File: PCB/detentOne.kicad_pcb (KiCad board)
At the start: 2 copper layers, 150 x 85 mm, 97 parts, among them CN1 S2B-PH-SM4-TB(LF)(SN), SW1 SW_Push, SW2 SW_Push, SW3 SW_Push, SW4 SW_Push, SW5 SW_Push, SW6 SW_Push, SW7 C92589, SW8 C92589, U1 BQ24074RGTR, U2 SGM2050XTRL20G/TR, U3 ESP32-S3-WROOM-1(N16R8), U4 TMC6300-LA-T_C5274455, U5 XY-GH1.25-7A61, U6 PCA9554ARGVR, U7 AS5047P-ATSM_C962063

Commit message: PCB layout done
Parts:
- removed R11: 0.05, Resistor_SMD:R_2010_5025Metric_Pad1.40x2.65mm_HandSolder
- removed the REF** at (89.0, 131.5)
- R1: value 2.2K -> 10K
- moved R13 124.0 mm to (157.0, 77.1), turned to 90 degrees
- moved R14 122.7 mm to (156.0, 77.1), turned to -90 degrees
- moved R15 121.4 mm to (155.0, 77.1), turned to -90 degrees
- moved R16 120.2 mm to (154.0, 77.1), turned to -90 degrees
- moved R17 119.1 mm to (153.0, 77.1), turned to 90 degrees
- moved R18 117.9 mm to (152.0, 77.1), turned to 90 degrees
- moved R19 106.5 mm to (139.0, 91.0)
- moved C13 104.8 mm to (140.0, 92.5), turned to 180 degrees
- moved C12 103.1 mm to (136.5, 97.5)
- moved C11 102.3 mm to (137.0, 90.5), turned to 90 degrees
- moved C10 100.6 mm to (134.0, 93.5), turned to 90 degrees
- moved C9 100.3 mm to (133.0, 93.5), turned to 90 degrees
- moved U4 90.8 mm to (137.2, 93.9)
- moved R1 76.4 mm to (130.4, 71.5)
- moved C4 70.8 mm to (122.5, 66.0)
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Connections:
- U3 pad 4: UH -> VL
- U3 pad 5: UL -> WL
- U3 pad 6: WH -> UL
- U3 pad 7: WL -> WH
- U3 pad 9: VL -> UH
- U4 pad 16: CURRENT_SENSE -> GND
- U4 pad 20: CURRENT_SENSE -> GND
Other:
- outline, holes or cut-outs redrawn
- board text added: "3V3 and GND, I2C pins go here"
- board text added: "Add outlines around modules like that cool PCB on X"
- board text added: "ON"

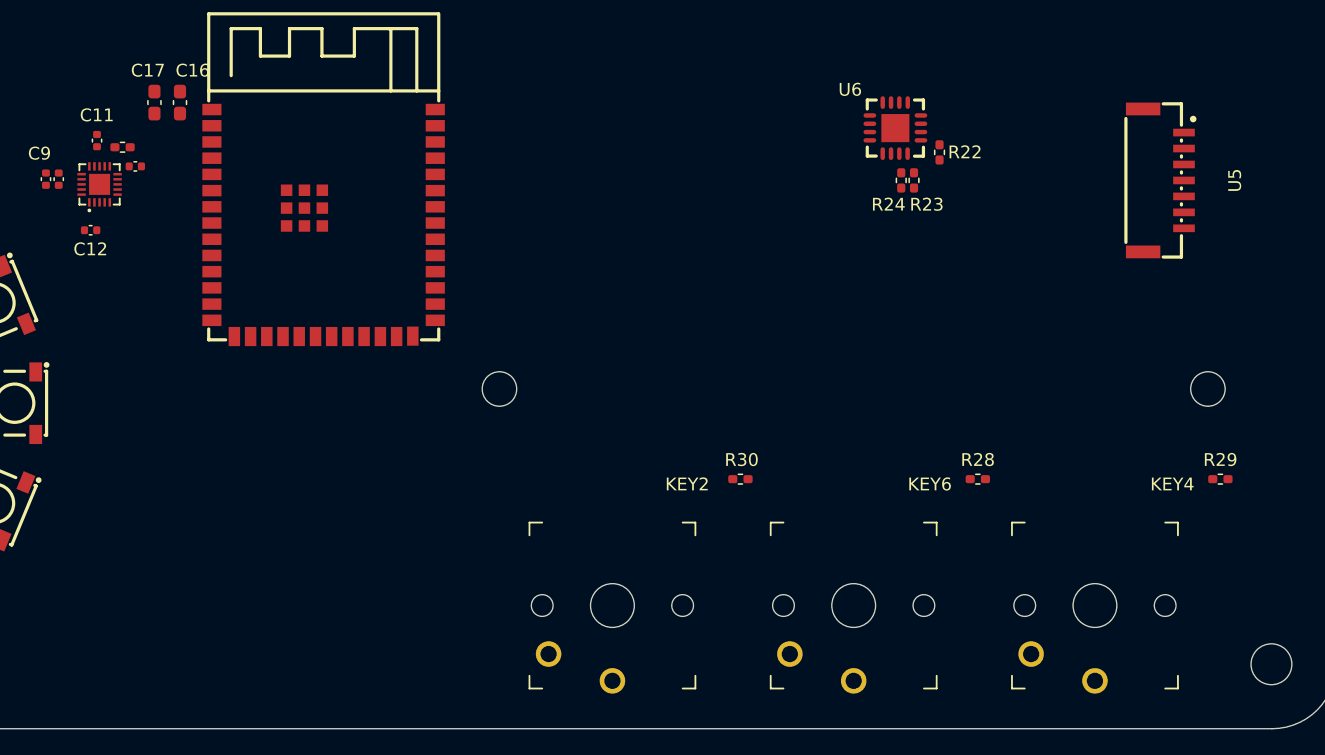
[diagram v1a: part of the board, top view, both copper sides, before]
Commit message: changes to PCB - next remove LiPO
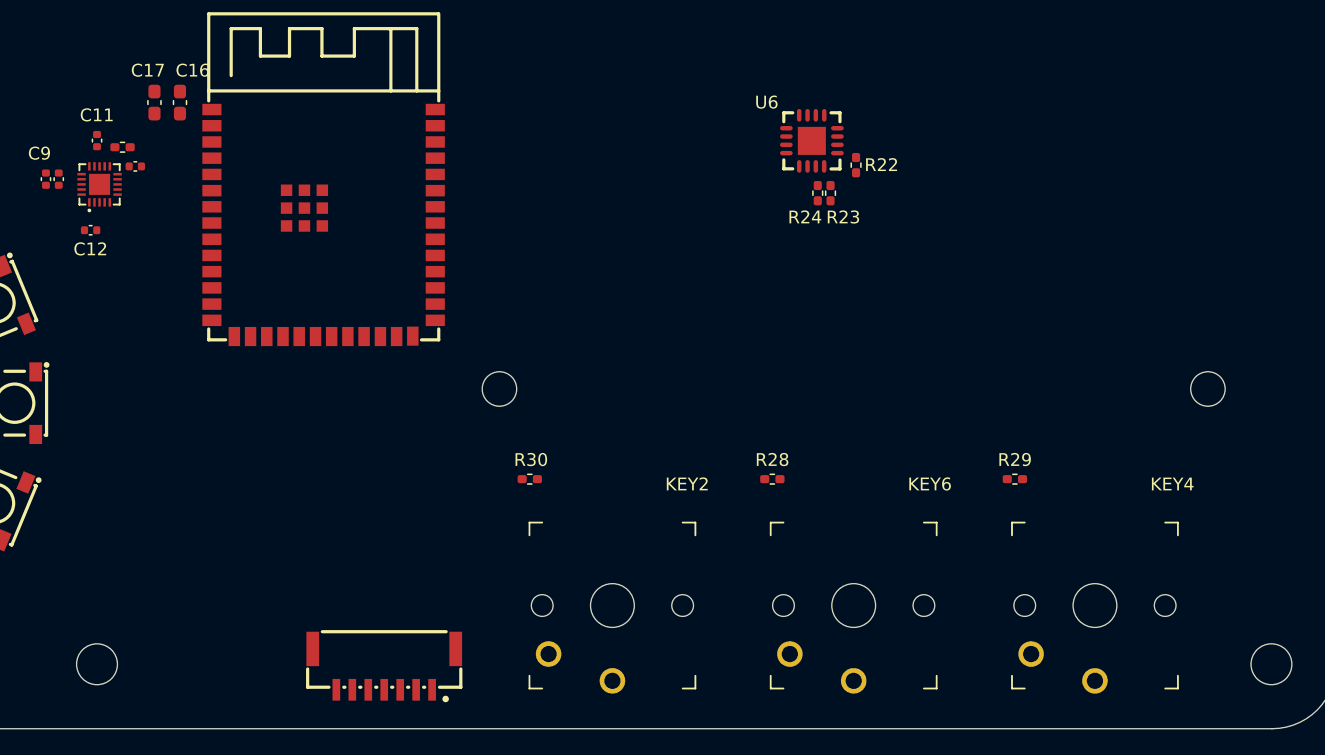
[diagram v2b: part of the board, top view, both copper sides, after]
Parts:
- added REF**: MountingHole_3.2mm_M3, MountingHole:MountingHole_3.2mm_M3, F.Cu at (137.0, 131.5)
- moved U5 72.1 mm to (159.5, 131.9), turned to 180 degrees
- moved R30 16.5 mm to (170.9, 117.0)
- moved R28 16.1 mm to (189.9, 117.0)
- moved R29 16.1 mm to (208.9, 117.0)
- moved R22 6.62 mm to (196.5, 92.4)
- moved R23 6.62 mm to (194.5, 94.6)
- moved R24 6.62 mm to (193.5, 94.6)
- moved U6 6.62 mm to (193.0, 90.5)
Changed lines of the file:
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@@
 	(footprint "Resistor_SMD:R_0402_1005Metric_Pad0.72x0.64mm_HandSolder"
 		(layer "F.Cu")
-		(at 203 91.4025 -90)
+		(at 196.46 92.4025 -90)
 		(descr "Resistor SMD 0402 (1005 Metric), square (rectangular) end terminal, IPC-7351 nominal with elongated pad for handsoldering. (Body size source: IPC-SM-782 page 72, https://www.pcb-3d.com/wordpress/wp-content/uploads/ipc-sm-782a_amendment_1_and_2.pdf), generated with kicad-footprint-generator")
 		(tags "resistor handsolder")
@@
 	(footprint "easyeda2kicad:VQFN-16_L4.0-W4.0-P0.65-TL-EP2.2"
 		(layer "F.Cu")
-		(at 199.54 89.5 -90)
+		(at 193 90.5 -90)
 		(property "Reference" "U6"
 			(at -3 3.54 180)
@@
 	(footprint "Resistor_SMD:R_0402_1005Metric_Pad0.72x0.64mm_HandSolder"
 		(layer "F.Cu")
-		(at 200 93.5975 -90)
+		(at 193.46 94.5975 -90)
 		(descr "Resistor SMD 0402 (1005 Metric), square (rectangular) end terminal, IPC-7351 nominal with elongated pad for handsoldering. (Body size source: IPC-SM-782 page 72, https://www.pcb-3d.com/wordpress/wp-content/uploads/ipc-sm-782a_amendment_1_and_2.pdf), generated with kicad-footprint-generator")
 		(tags "resistor handsolder")
@@
 	(footprint "Resistor_SMD:R_0402_1005Metric_Pad0.72x0.64mm_HandSolder"
 		(layer "F.Cu")
-		(at 206 117 180)
+		(at 189.9025 117 180)
 		(descr "Resistor SMD 0402 (1005 Metric), square (rectangular) end terminal, IPC-7351 nominal with elongated pad for handsoldering. (Body size source: IPC-SM-782 page 72, https://www.pcb-3d.com/wordpress/wp-content/uploads/ipc-sm-782a_amendment_1_and_2.pdf), generated with kicad-footprint-generator")
 		(tags "resistor handsolder")
@@
 	(footprint "Resistor_SMD:R_0402_1005Metric_Pad0.72x0.64mm_HandSolder"
 		(layer "F.Cu")
-		(at 225 117 180)
+		(at 208.9025 117 180)
 		(descr "Resistor SMD 0402 (1005 Metric), square (rectangular) end terminal, IPC-7351 nominal with elongated pad for handsoldering. (Body size source: IPC-SM-782 page 72, https://www.pcb-3d.com/wordpress/wp-content/uploads/ipc-sm-782a_amendment_1_and_2.pdf), generated with kicad-footprint-generator")
 		(tags "resistor handsolder")
@@
 		(model "easyeda2kicad/easyeda2kicad.3dshapes/USB-C-SMD_TYPE-C-6PIN-2MD-073.wrl"
 			(offset
-				(xyz 0 -1.2 0.9)
+				(xyz 0 -1.2 1.4)
 			)
 			(scale
@@
 			)
 			(rotate
-				(xyz 0 0 0)
+				(xyz -0 -0 -0)
 			)
 		)
@@
 		)
 	)
+	(footprint "MountingHole:MountingHole_3.2mm_M3"
+		(layer "F.Cu")
+		(at 137 131.5)
+		(descr "Mounting Hole 3.2mm, M3, no annular, generated by kicad-footprint-generator mountinghole.py")
+		(tags "mountinghole M3")
+		(property "Reference" "REF**"
+			(at 0 -4.15 0)
+			(layer "F.SilkS")
+			(hide yes)
+			(effects
+				(font
+					(size 1 1)
+					(thickness 0.15)
+				)
+			)
+		)
+		(property "Value" "MountingHole_3.2mm_M3"
+			(at 0 4.15 0)
+			(layer "F.Fab")
+			(hide yes)
+			(effects
+				(font
+					(size 1 1)
+					(thickness 0.15)
+				)
+			)
+		)
+		(property "Datasheet" ""
+			(at 0 0 0)
+			(layer "F.Fab")
+			(hide yes)
+			(effects
+				(font
+					(size 1.27 1.27)
+					(thickness 0.15)
+				)
+			)
+		)
+		(property "Description" ""
+			(at 0 0 0)
+			(layer "F.Fab")
+			(hide yes)
+			(effects
+				(font
+					(size 1.27 1.27)
+					(thickness 0.15)
+				)
+			)
+		)
+		(attr exclude_from_pos_files exclude_from_bom)
+		(fp_circle
+			(center 0 0)
+			(end 3.2 0)
+			(stroke
+				(width 0.15)
+				(type solid)
+			)
+			(fill no)
+			(layer "Cmts.User")
+		)
+		(fp_circle
+			(center 0 0)
+			(end 3.45 0)
+			(stroke
+				(width 0.05)
+				(type solid)
+			)
+			(fill no)
+			(layer "F.CrtYd")
+		)
+		(pad "" np_thru_hole circle
+			(at 0 0)
+			(size 3.2 3.2)
+			(drill 3.2)
+			(layers "*.Cu" "*.Mask")
+		)
+		(embedded_fonts no)
+	)
 	(footprint "Resistor_SMD:R_0402_1005Metric_Pad0.72x0.64mm_HandSolder"
 		(layer "F.Cu")
@@
 	(footprint "Resistor_SMD:R_0402_1005Metric_Pad0.72x0.64mm_HandSolder"
 		(layer "F.Cu")
-		(at 187.4025 117 180)
+		(at 170.9025 117 180)
 		(descr "Resistor SMD 0402 (1005 Metric), square (rectangular) end terminal, IPC-7351 nominal with elongated pad for handsoldering. (Body size source: IPC-SM-782 page 72, https://www.pcb-3d.com/wordpress/wp-content/uploads/ipc-sm-782a_amendment_1_and_2.pdf), generated with kicad-footprint-generator")
 		(tags "resistor handsolder")
@@
 	(footprint "easyeda2kicad:CONN-SMD_7P-P1.25_XYECONN_XY-GH1.25-7A61"
 		(layer "F.Cu")
-		(at 220.55 93.6 -90)
+		(at 159.5 131.9 180)
 		(property "Reference" "U5"
-			(at 0 -5.6 90)
+			(at 0 -5.6 0)
 			(layer "F.SilkS")
+			(hide yes)
 			(effects
 				(font
@@
 		)
 		(property "Value" "XY-GH1.25-7A61"
-			(at 0 5.6 90)
+			(at 0 5.6 0)
 			(layer "F.Fab")
 			(hide yes)
@@
 		)
 		(property "Datasheet" ""
-			(at 0 0 90)
+			(at 0 0 0)
 			(layer "F.Fab")
 			(hide yes)
@@
 		)
 		(property "Description" ""
-			(at 0 0 90)
+			(at 0 0 0)
 			(layer "F.Fab")
 			(hide yes)
@@
 		)
 		(property "LCSC Part" "C19272064"
-			(at 0 0 270)
+			(at 0 0 180)
 			(unlocked yes)
 			(layer "F.Fab")
@@
 		(attr smd)
 		(fp_line
-			(start 4.85 2.95)
-			(end -4.85 2.95)
+			(start 6 -1.4)
+			(end 6 0.03)
 			(stroke
 				(width 0.25)
@@
 		)
 		(fp_line
-			(start -6 -1.4)
-			(end -6 0.03)
+			(start 6 -1.4)
+			(end 4.33 -1.4)
 			(stroke
 				(width 0.25)
@@
 		)
 		(fp_line
-			(start -4.33 -1.4)
-			(end -6 -1.4)
+			(start 4.85 2.95)
+			(end -4.85 2.95)
 			(stroke
 				(width 0.25)
@@
 		)
 		(fp_line
-			(start -3.08 -1.4)
-			(end -3.17 -1.4)
+			(start 3.17 -1.4)
+			(end 3.08 -1.4)
 			(stroke
 				(width 0.25)
@@
 		)
 		(fp_line
-			(start -1.83 -1.4)
-			(end -1.92 -1.4)
+			(start 1.92 -1.4)
+			(end 1.83 -1.4)
 			(stroke
 				(width 0.25)
@@
 		)
 		(fp_line
-			(start -0.58 -1.4)
-			(end -0.67 -1.4)
+			(start 0.67 -1.4)
+			(end 0.58 -1.4)
 			(stroke
 				(width 0.25)
@@
 		)
 		(fp_line
-			(start 0.67 -1.4)
-			(end 0.58 -1.4)
+			(start -0.58 -1.4)
+			(end -0.67 -1.4)
 			(stroke
 				(width 0.25)
@@
 		)
 		(fp_line
-			(start 1.92 -1.4)
-			(end 1.83 -1.4)
+			(start -1.83 -1.4)
+			(end -1.92 -1.4)
 			(stroke
 				(width 0.25)
@@
 		)
 		(fp_line
-			(start 3.17 -1.4)
-			(end 3.08 -1.4)
+			(start -3.08 -1.4)
+			(end -3.17 -1.4)
 			(stroke
 				(width 0.25)
@@
 		)
 		(fp_line
-			(start 6 -1.4)
-			(end 6 0.03)
+			(start -4.33 -1.4)
+			(end -6 -1.4)
 			(stroke
 				(width 0.25)
@@
 		)
 		(fp_line
-			(start 6 -1.4)
-			(end 4.33 -1.4)
+			(start -6 -1.4)
+			(end -6 0.03)
 			(stroke
 				(width 0.25)
@@
 		)
 		(fp_text user "${REFERENCE}"
-			(at 0 0 90)
+			(at 0 0 0)
 			(layer "F.Fab")
 			(effects
@@
 		)
 		(pad "1" smd rect
-			(at -3.75 -1.6 270)
+			(at -3.75 -1.6 180)
 			(size 0.6 1.7)
 			(layers "F.Cu" "F.Mask" "F.Paste")
@@
 		)
 		(pad "2" smd rect
-			(at -2.5 -1.6 270)
+			(at -2.5 -1.6 180)
 			(size 0.6 1.7)
 			(layers "F.Cu" "F.Mask" "F.Paste")
@@
 		)
 		(pad "3" smd rect
-			(at -1.25 -1.6 270)
+			(at -1.25 -1.6 180)
 			(size 0.6 1.7)
 			(layers "F.Cu" "F.Mask" "F.Paste")
@@
 		)
 		(pad "4" smd rect
-			(at 0 -1.6 270)
+			(at 0 -1.6 180)
 			(size 0.6 1.7)
 			(layers "F.Cu" "F.Mask" "F.Paste")
@@
 		)
 		(pad "5" smd rect
-			(at 1.25 -1.6 270)
+			(at 1.25 -1.6 180)
 			(size 0.6 1.7)
 			(layers "F.Cu" "F.Mask" "F.Paste")
@@
 		)
 		(pad "6" smd rect
-			(at 2.5 -1.6 270)
+			(at 2.5 -1.6 180)
 			(size 0.6 1.7)
 			(layers "F.Cu" "F.Mask" "F.Paste")
@@
 		)
 		(pad "7" smd rect
-			(at 3.75 -1.6 270)
+			(at 3.75 -1.6 180)
 			(size 0.6 1.7)
 			(layers "F.Cu" "F.Mask" "F.Paste")
@@
 		)
 		(pad "8" smd rect
-			(at 5.6 1.6 90)
+			(at 5.6 1.6)
 			(size 1 2.7)
 			(layers "F.Cu" "F.Mask" "F.Paste")
@@
 		)
 		(pad "9" smd rect
-			(at -5.6 1.6 270)
+			(at -5.6 1.6 180)
 			(size 1 2.7)
 			(layers "F.Cu" "F.Mask" "F.Paste")
@@
 	(footprint "Resistor_SMD:R_0402_1005Metric_Pad0.72x0.64mm_HandSolder"
 		(layer "F.Cu")
-		(at 201 93.5975 -90)
+		(at 194.46 94.5975 -90)
 		(descr "Resistor SMD 0402 (1005 Metric), square (rectangular) end terminal, IPC-7351 nominal with elongated pad for handsoldering. (Body size source: IPC-SM-782 page 72, https://www.pcb-3d.com/wordpress/wp-content/uploads/ipc-sm-782a_amendment_1_and_2.pdf), generated with kicad-footprint-generator")
 		(tags "resistor handsolder")
@@
 	)
 	(gr_text "3V3 and GND, I2C pins go here"
-		(at 139 133 0)
+		(at 137 118 0)
 		(layer "User.1")
 		(effects

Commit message: PCB changes - todo remove LIPO
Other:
- board text added: "Remove Lipo Functionality"
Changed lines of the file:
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@@
+		)
+	)
+	(gr_text "Remove Lipo Functionality"
+		(at 152.5 40.5 0)
+		(layer "User.1")
+		(effects
+			(font
+				(size 1 1)
+				(thickness 0.15)
+			)
+			(justify left bottom)
 		)
 	)

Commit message: pcb changes
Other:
- board text added: "Remove Lipo Functionality!"
- board text removed: "Remove Lipo Functionality"
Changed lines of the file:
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@@
 		)
 	)
-	(gr_text "Remove Lipo Functionality"
-		(at 152.5 40.5 0)
+	(gr_text "Remove Lipo Functionality!"
+		(at 130 49.5 0)
 		(layer "User.1")
 		(effects

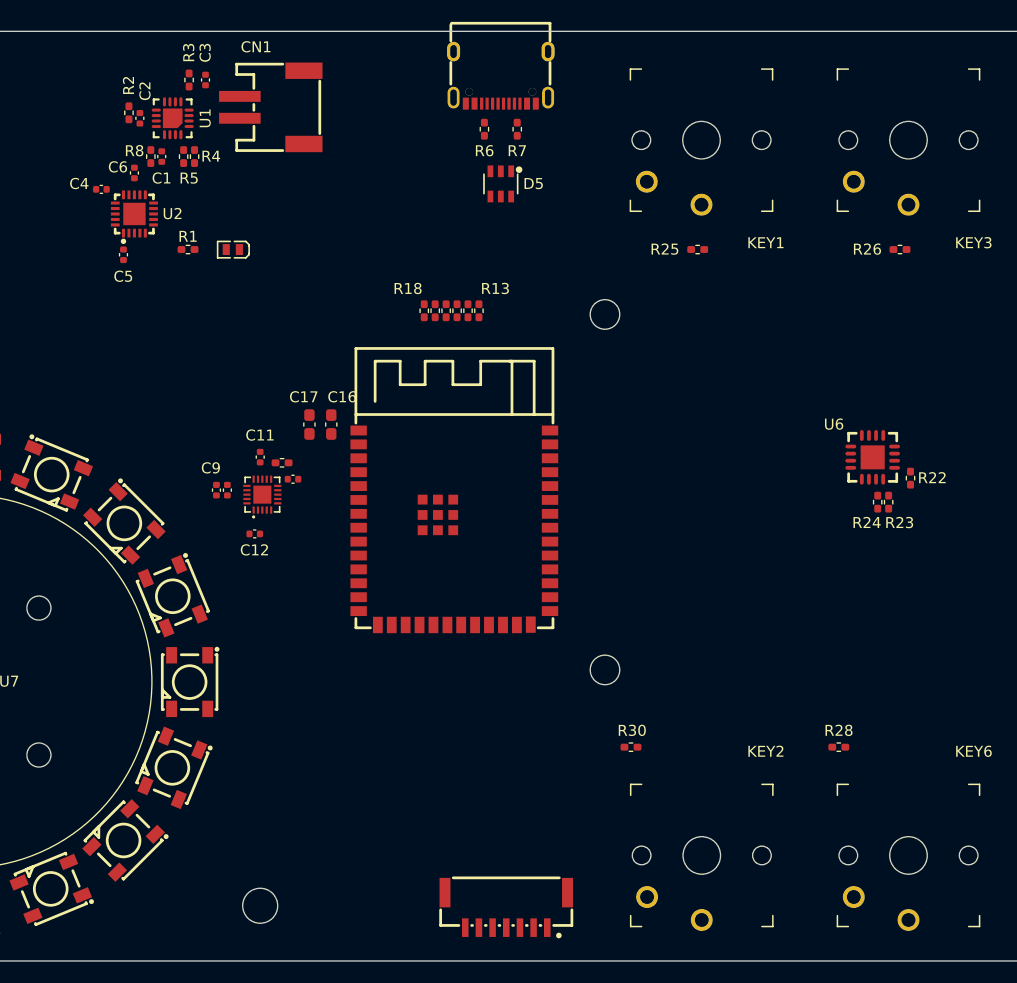
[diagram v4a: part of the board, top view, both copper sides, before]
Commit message: removed lipo circuitry
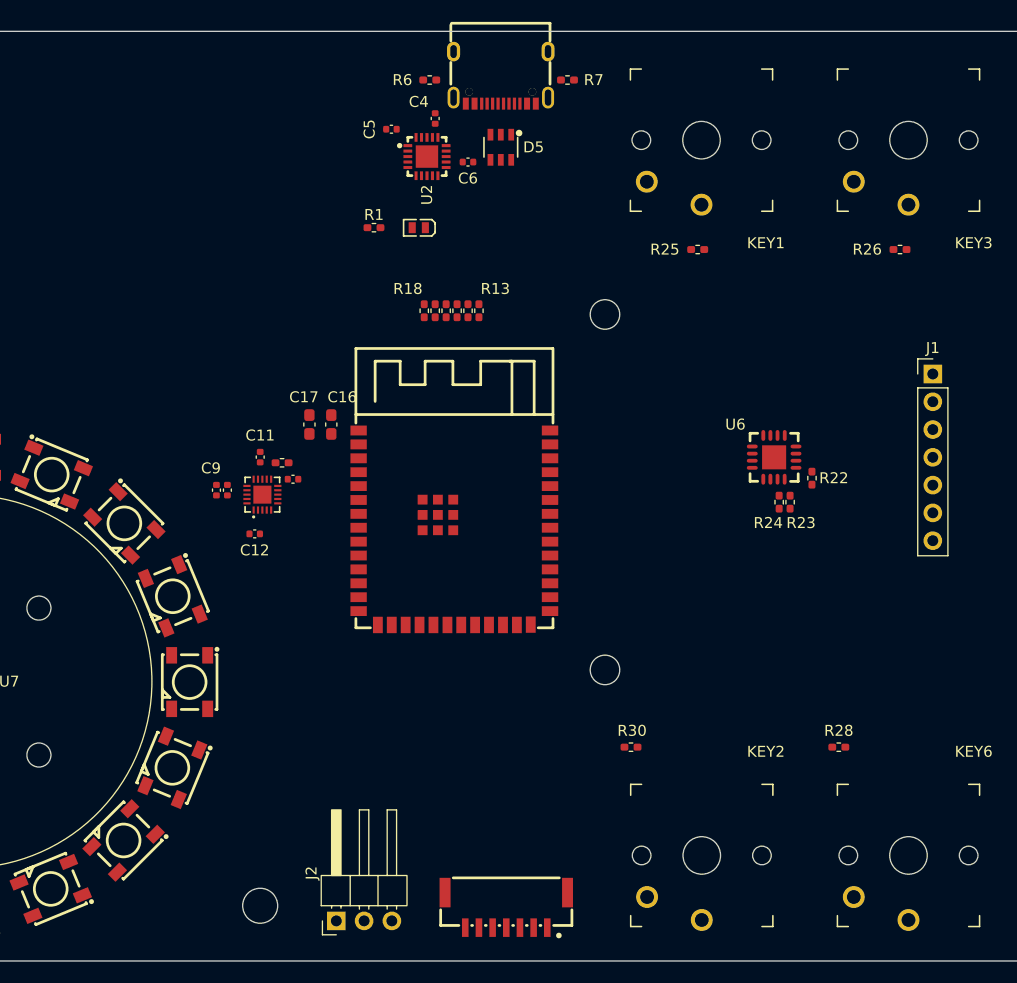
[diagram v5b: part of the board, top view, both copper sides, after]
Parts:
- removed C1, C2: 4.7uF 10V, Capacitor_SMD:C_0402_1005Metric
- removed C3: 1uF 10V, Capacitor_SMD:C_0402_1005Metric
- removed CN1: S2B-PH-SM4-TB(LF)(SN), easyeda2kicad:CONN-SMD_P2.00_S2B-PH-SM4-TB-LF-SN
- removed R2, R3: 5.1K, Resistor_SMD:R_0402_1005Metric_Pad0.72x0.64mm_HandSolder
- removed R4: 10K, Resistor_SMD:R_0402_1005Metric_Pad0.72x0.64mm_HandSolder
- removed R5: 2.21K, Resistor_SMD:R_0402_1005Metric_Pad0.72x0.64mm_HandSolder
- removed R8: 3.09K, Resistor_SMD:R_0402_1005Metric_Pad0.72x0.64mm_HandSolder
- removed U1: BQ24074RGTR, easyeda2kicad:QFN-16_L3.0-W3.0-P0.50-TL-EP1.7
- added J1: Conn_01x07, Connector_PinHeader_2.54mm:PinHeader_1x07_P2.54mm_Vertical, F.Cu at (198.5, 82.9)
- added J2: Conn_01x03, Connector_PinHeader_2.54mm:PinHeader_1x03_P2.54mm_Horizontal, F.Cu at (144.0, 132.9)
- moved C4 31.2 mm to (153.0, 59.5), turned to -90 degrees
- moved C6 30.5 mm to (156.0, 63.5), turned to 180 degrees
- moved U2 27.3 mm to (152.2, 63.0), turned to -90 degrees
- moved C5 27.1 mm to (149.0, 60.5), turned to 0 degrees
- moved LED1 17.1 mm to (151.5, 69.5)
- moved R1 17.1 mm to (147.4, 69.5)
- moved R22 9.01 mm to (187.4, 92.4)
- moved R23 9.01 mm to (185.4, 94.6)
- moved R24 9.01 mm to (184.4, 94.6)
- moved U6 9.01 mm to (184.0, 90.5)
- moved R6 6.73 mm to (152.5, 56.0), turned to 180 degrees
- moved R7 6.43 mm to (165.1, 56.0), turned to 0 degrees
- moved D5 3.35 mm to (159.0, 62.1)
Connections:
- C4 pad 2: /PowerManagement/VSYS -> /PowerManagement/5V
- U2 pad 14: /PowerManagement/VSYS -> /PowerManagement/5V
- U2 pad 15: /PowerManagement/VSYS -> /PowerManagement/5V
- U2 pad 16: /PowerManagement/VSYS -> /PowerManagement/5V
- U2 pad 17: /PowerManagement/VSYS -> /PowerManagement/5V
